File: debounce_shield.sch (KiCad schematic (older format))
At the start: 34 parts, among them J2 RPi_GPIO, P1 CONN_12, P2 CONN_2, U1 40106

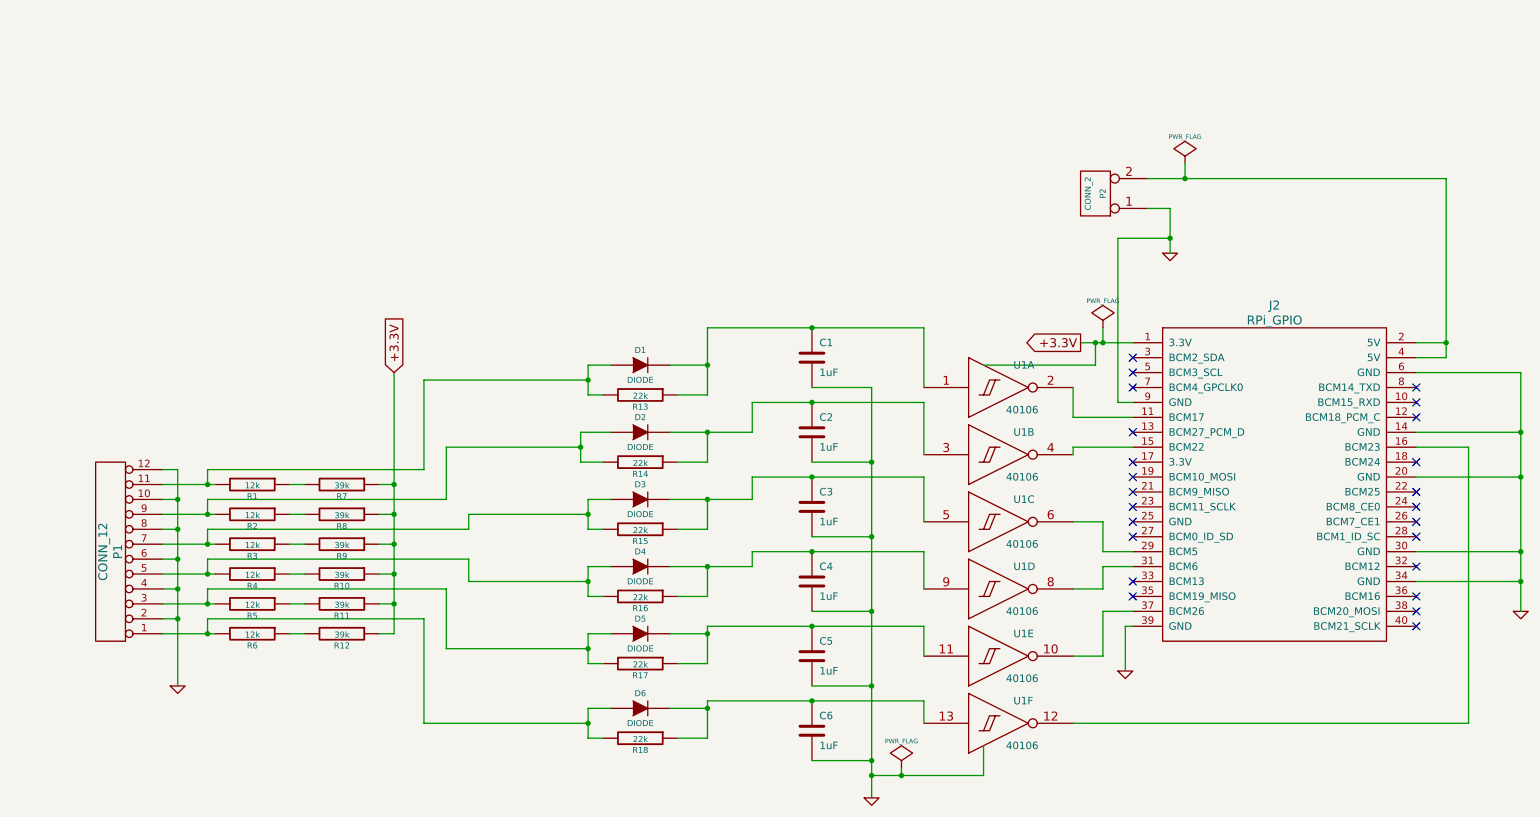
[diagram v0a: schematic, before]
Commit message: Add HAT EEPROM & 5V feed diode.
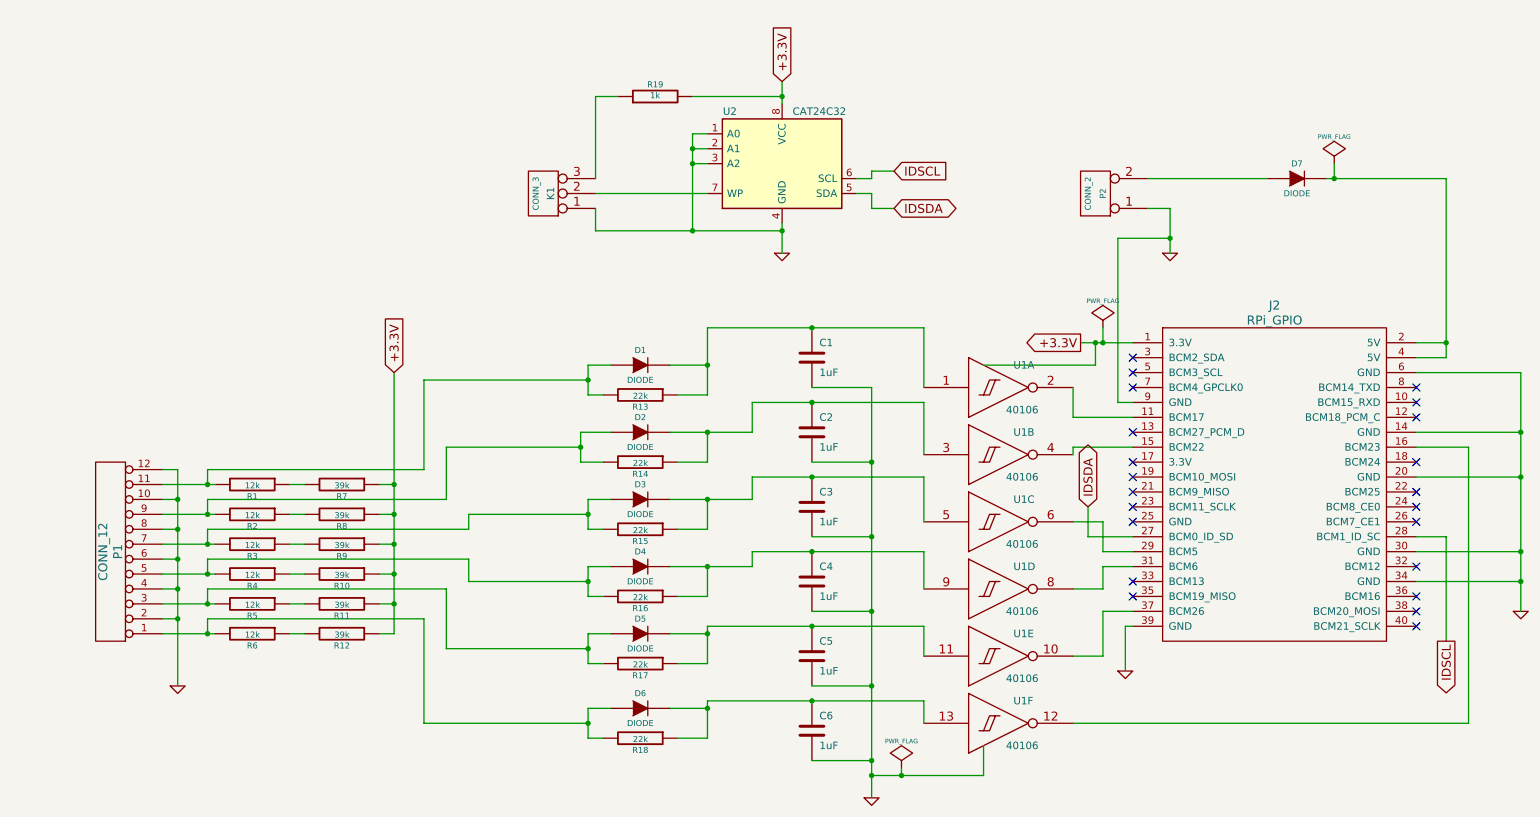
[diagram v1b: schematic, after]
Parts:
- added D7: DIODE, Diodes_SMD:D_0805, symbol DIODE
- added K1: CONN_3, Pin_Headers:Pin_Header_Straight_1x03_Pitch2.54mm, symbol CONN_3
- added R19: 1k, Resistors_SMD:R_0805_HandSoldering, symbol R
- added U2: CAT24C32, SMD_Packages:SOIC-8-N, symbol CAT24C32
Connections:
- net GND: now also K1.1 (P1), U2.1 (A0), U2.2 (A1), U2.3 (A2), U2.4 (GND)
- net VDD: now also R19.2, U2.8 (VCC)
- net at J2.2 (5V), J2.4 (5V): now also D7.2 (K); no longer P2.2 (PM)
- net IDSDA: now reaches J2.27 (BCM0_ID_SD)
- net IDSDA: now also U2.5 (SDA)
- net IDSCL: now reaches J2.28 (BCM1_ID_SC)
- net IDSCL: now also U2.6 (SCL)
- new net: D7.1 (A), P2.2 (PM)
- new net: K1.2 (PM), U2.7 (WP)
- new net: K1.3 (P3), R19.1
- no-connect marks 24 -> 22

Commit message: Add ID_SC, ID_SD pull-up resistors.
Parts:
- added R20, R21: 3.9k, Resistors_SMD:R_0805_HandSoldering, symbol R
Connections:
- net IDSCL: now also R20.2
- net IDSDA: now also R21.1
- net VDD: now also R20.1, R21.2
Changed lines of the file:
@@
 Text GLabel 10250 4650 3    60   Output ~ 0
 IDSCL
-Text GLabel 6550 1500 2    60   Input ~ 0
+Text GLabel 6800 1500 2    60   Input ~ 0
 IDSCL
-Text GLabel 6550 1750 2    60   BiDi ~ 0
+Text GLabel 6800 1750 2    60   BiDi ~ 0
 IDSDA
 $Comp
@@
 	10250 3950 10250 4650
 Wire Wire Line
-	6550 1500 6400 1500
+	6400 1500 6800 1500
 Wire Wire Line
 	6400 1500 6400 1550
@@
 	6400 1550 6300 1550
 Wire Wire Line
-	6550 1750 6400 1750
+	6400 1750 6800 1750
 Wire Wire Line
 	6400 1750 6400 1650
@@
 	6400 1650 6300 1650
 Wire Wire Line
-	5200 1000 5800 1000
+	5200 1000 6650 1000
 Connection ~ 5800 1000
 Wire Wire Line
@@
 	9500 1450 9500 1550
 Connection ~ 9500 1550
+$Comp
+L R R20
+U 1 1 5AAFD3AE
+P 6650 1250
+F 0 "R20" V 6730 1250 40  0000 C CNN
+F 1 "3.9k" V 6657 1251 40  0000 C CNN
+F 2 "Resistors_SMD:R_0805_HandSoldering" V 6580 1250 30  0001 C CNN
+F 3 "" H 6650 1250 30  0000 C CNN
+	1    6650 1250
+	1    0    0    -1
+$EndComp
+$Comp
+L R R21
+U 1 1 5AAFD443
+P 6650 2000
+F 0 "R21" V 6730 2000 40  0000 C CNN
+F 1 "3.9k" V 6657 2001 40  0000 C CNN
+F 2 "Resistors_SMD:R_0805_HandSoldering" V 6580 2000 30  0001 C CNN
+F 3 "" H 6650 2000 30  0000 C CNN
+	1    6650 2000
+	1    0    0    -1
+$EndComp
+Connection ~ 6650 1500
+Connection ~ 6650 1750
+Text GLabel 6850 2250 2    60   Input ~ 0
++3.3V
+Wire Wire Line
+	6850 2250 6650 2250
 $EndSCHEMATC

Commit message: Add optocoupler & other improvements.
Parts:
- added R22, R23, R24, R25, R26, R27: 191, Resistor_SMD:R_1206_3216Metric_Pad1.42x1.75mm_HandSolder, symbol Device:R_Small
- added U3, U4, U5: LTV-824, Package_DIP:DIP-8_W7.62mm, symbol Isolator:LTV-824
- C1, C2, C3, C4, C5, C6: footprint Capacitors_SMD:C_0805_HandSoldering -> Capacitor_SMD:C_0805_2012Metric_Pad1.15x1.40mm_HandSolder; symbol C -> debounce_shield-rescue:C
- D1, D2, D3, D4, D5, D6, D7: footprint Diodes_SMD:D_0805 -> Diode_SMD:D_0805_2012Metric_Pad1.15x1.40mm_HandSolder; symbol DIODE -> debounce_shield-rescue:DIODE
- J2: symbol RPi_GPIO -> debounce_shield-rescue:RPi_GPIO
- K1: footprint Pin_Headers:Pin_Header_Straight_1x03_Pitch2.54mm -> Connector_PinHeader_2.54mm:PinHeader_1x03_P2.54mm_Vertical; symbol CONN_3 -> debounce_shield-rescue:CONN_3
- P1: footprint TerminalBlocks_Phoenix:TerminalBlock_Phoenix_MPT-2.54mm_12pol -> TerminalBlock_Phoenix:TerminalBlock_Phoenix_MPT-0,5-12-2.54_1x12_P2.54mm_Horizontal; symbol CONN_12 -> debounce_shield-rescue:CONN_12
- P2: footprint TerminalBlocks_Phoenix:TerminalBlock_Phoenix_MPT-2.54mm_2pol -> TerminalBlock_Phoenix:TerminalBlock_Phoenix_MPT-0,5-2-2.54_1x02_P2.54mm_Horizontal; symbol CONN_2 -> debounce_shield-rescue:CONN_2
- R1, R10, R11, R12, R13, R14, R15, R16, R17, R18, R2, R3, R4, R5, R6, R7, R8, R9: footprint Capacitors_SMD:C_0805_HandSoldering -> Resistor_SMD:R_0805_2012Metric_Pad1.15x1.40mm_HandSolder; symbol R -> debounce_shield-rescue:R
- R19, R20, R21: footprint Resistors_SMD:R_0805_HandSoldering -> Resistor_SMD:R_0805_2012Metric_Pad1.15x1.40mm_HandSolder; symbol R -> debounce_shield-rescue:R
- U1: footprint SMD_Packages:SOIC-14_N -> Package_SO:SOIC-14_3.9x8.7mm_P1.27mm; symbol 40106 -> debounce_shield-rescue:40106
- U2: footprint SMD_Packages:SOIC-8-N -> Package_SO:SOIC-8_3.9x4.9mm_P1.27mm; symbol CAT24C32 -> debounce_shield-rescue:CAT24C32
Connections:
- net GND: now also U3.2, U3.4, U3.5, U3.7, U4.2, U4.4, U4.5, U4.7, U5.2, U5.4, U5.5, U5.7; no longer P1.10 (P10), P1.12 (P12), P1.2 (P2), P1.4 (P4), P1.6 (P6), P1.8 (P8)
- net +5V: now reaches D7.2 (K), J2.2 (5V), J2.4 (5V)
- net +5V: now also P1.10 (P10), P1.12 (P12), P1.2 (P2), P1.4 (P4), P1.6 (P6), P1.8 (P8)
- net at D1.1 (A), R1.2, R13.2: now also U3.6; no longer P1.11 (P11)
- net at D2.1 (A), R14.2, R2.2: now also U3.8; no longer P1.9 (P9)
- net at D3.1 (A), R15.2, R3.2: now also U4.6; no longer P1.7 (P7)
- net at D4.1 (A), R16.2, R4.2: now also U4.8; no longer P1.5 (P5)
- net at D5.1 (A), R17.2, R5.2: now also U5.6; no longer P1.3 (P3)
- net at D6.1 (A), R18.2, R6.2: now also U5.8; no longer P1.1 (P1)
- new net: P1.1 (P1), R27.2
- new net: P1.11 (P11), R22.2
- new net: P1.3 (P3), R26.2
- new net: P1.5 (P5), R25.2
- new net: P1.7 (P7), R24.2
- new net: P1.9 (P9), R23.2
- new net: R22.1, U3.3
- new net: R23.1, U3.1
- new net: R24.1, U4.3
- new net: R25.1, U4.1
- new net: R26.1, U5.3
- new net: R27.1, U5.1
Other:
- moved on the sheet: P1, R1, R10, R11, R12, R2, R3, R4, R5, R6, R7, R8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
